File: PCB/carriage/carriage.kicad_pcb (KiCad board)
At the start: 2 copper layers, 135 x 26 mm, 8 parts

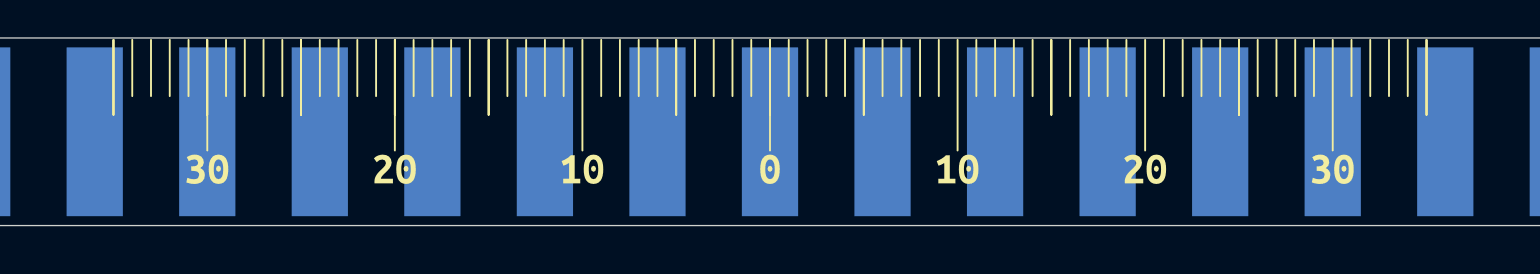
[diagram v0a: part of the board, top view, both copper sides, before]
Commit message: update design with lessons learned from pilot production
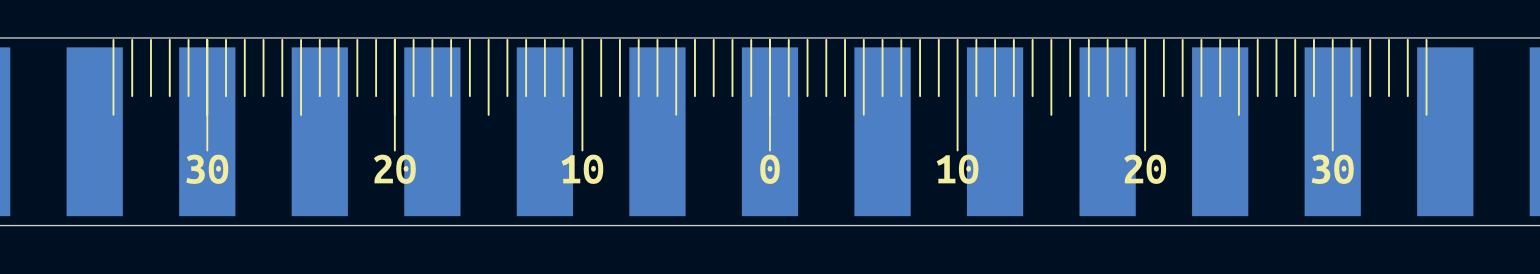
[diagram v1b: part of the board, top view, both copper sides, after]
